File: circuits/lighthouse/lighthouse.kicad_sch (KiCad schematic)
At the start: 45 parts, among them J1 USB_C_Receptacle_USB2.0_14P, J2 Conn_01x03_Socket, Q1 S9013, Q4 SS8050, Q5 SS8050, U10 CP2102-GMR, U2 AMS1117-3.3, U7 ESP32-WROOM-32

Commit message: Ready to go circuit (what a naive thing to say)
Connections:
- net +3.3V: now also R34.2, R8.1
- net +5V: no longer R34.2, R8.1
- net ACTIVE_SCAN: now also U7.34 (RXD0/IO3); no longer U7.30 (IO18)
- net ESP24: now also U7.25 (IO0); no longer U7.24 (IO2)
- net ESP25: now also U7.10 (IO25); no longer U7.25 (IO0)
- net ESP34: now also U7.23 (IO15); no longer U7.34 (RXD0/IO3)
- net ESP35: now also U7.24 (IO2); no longer U7.35 (TXD0/IO1)
- net MQTT_STS: now also U7.26 (IO4); no longer U7.29 (IO5)
- net PIR: now also U7.31 (IO19); no longer U7.8 (IO32)
- net RFID_PW: now also U7.29 (IO5); no longer U7.33 (IO21)
- net RFID_PW_SENSE: now also U7.30 (IO18); no longer U7.36 (IO22)
- net SCAN_DETECTED: now also U7.35 (TXD0/IO1); no longer U7.31 (IO19)
- net WIFI_STS: now also U7.33 (IO21); no longer U7.37 (IO23)
- net at R34.1, SCAN_TGL1.2: now also U7.37 (IO23); no longer U7.6 (IO34)
- net at R8.2, STATUS/SETUP1.2: now also U7.36 (IO22); no longer U7.7 (IO35)
- no-connect marks 25 -> 22
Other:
- moved on the sheet: R21, R34, R8, SCAN_TGL1, STATUS/SETUP1

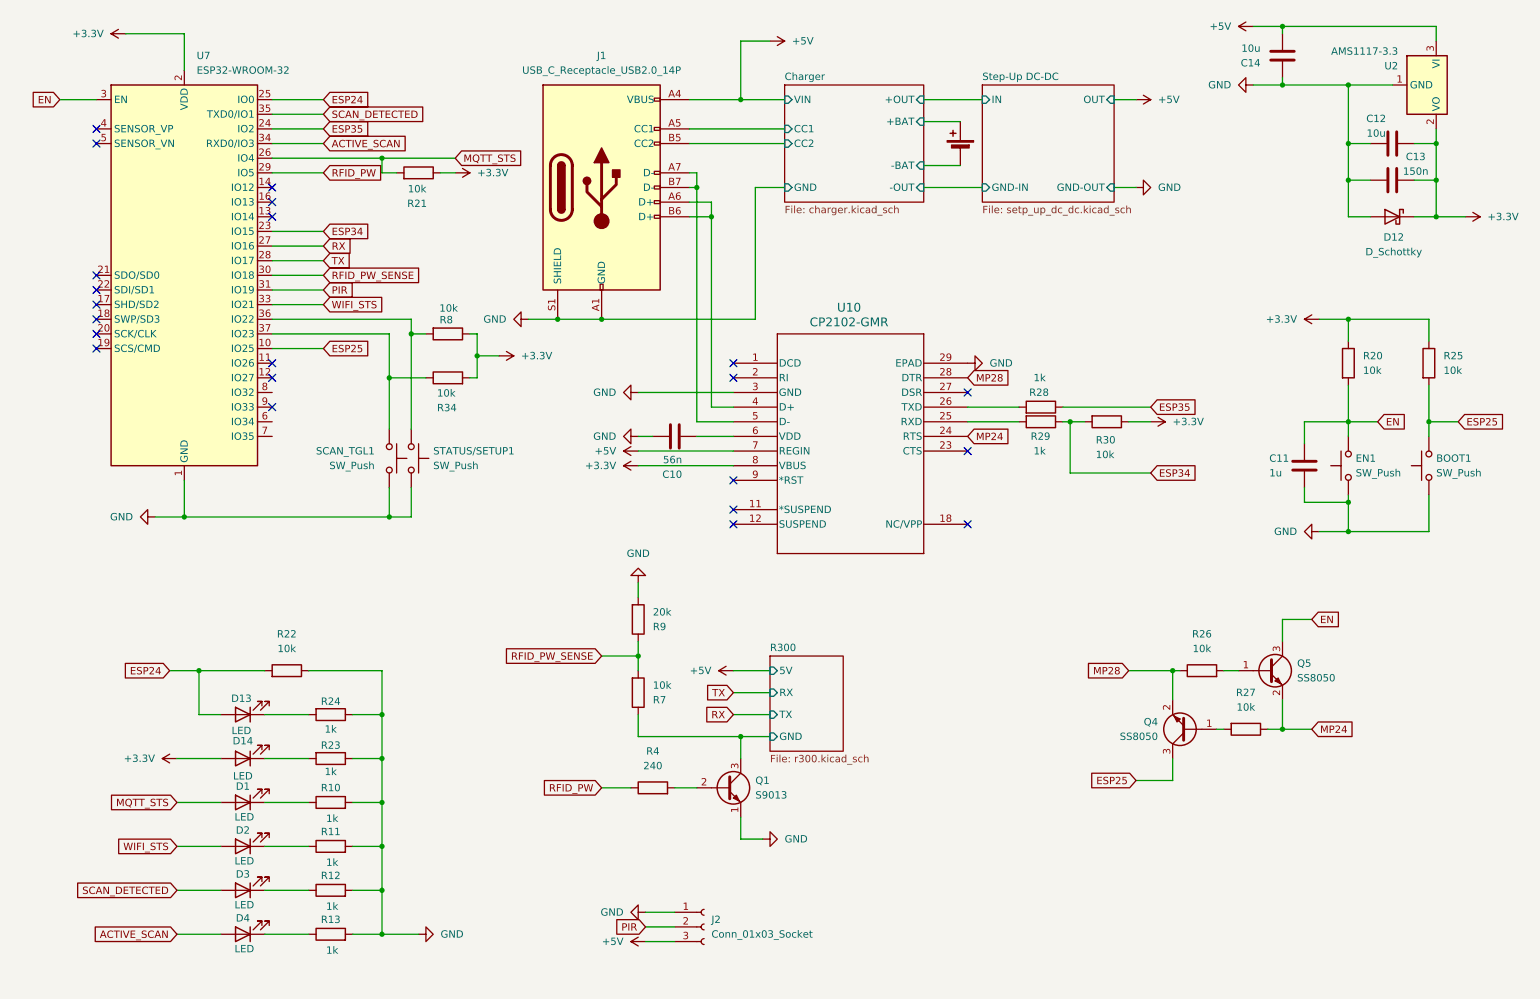
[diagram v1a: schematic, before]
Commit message: Adjusted visa sizes
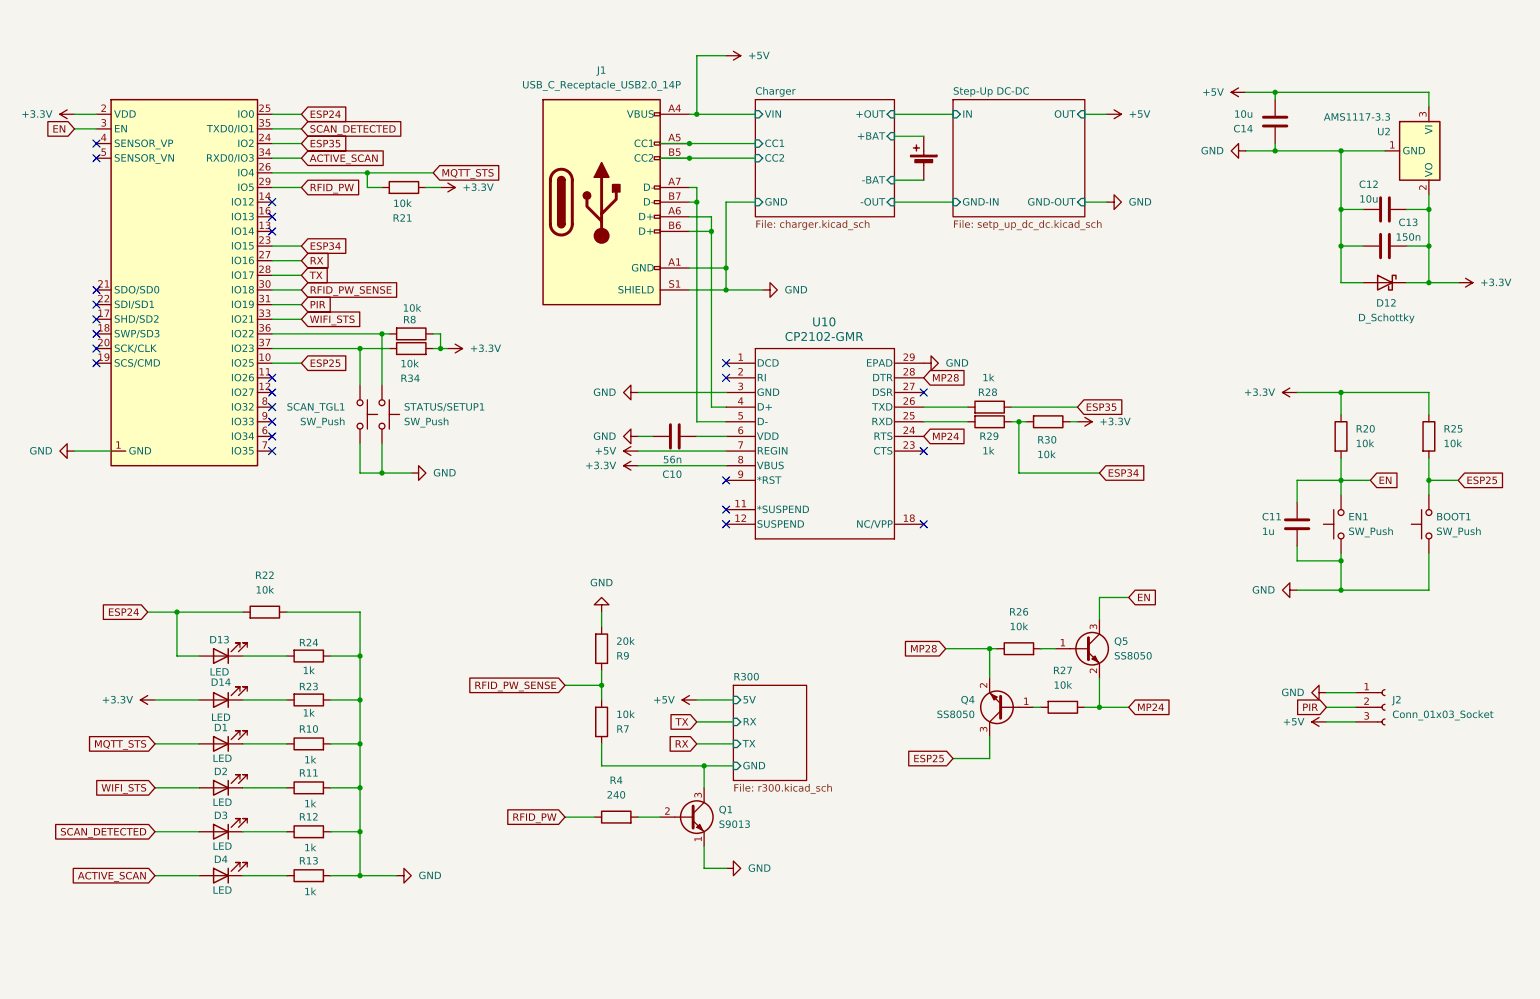
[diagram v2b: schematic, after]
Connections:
- net GND: now also U7.32 (NC)
- no-connect marks 22 -> 25
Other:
- moved on the sheet: BOOT1, C11, C12, C13, C14, D1, D12, D13, D14, D2, D3, D4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

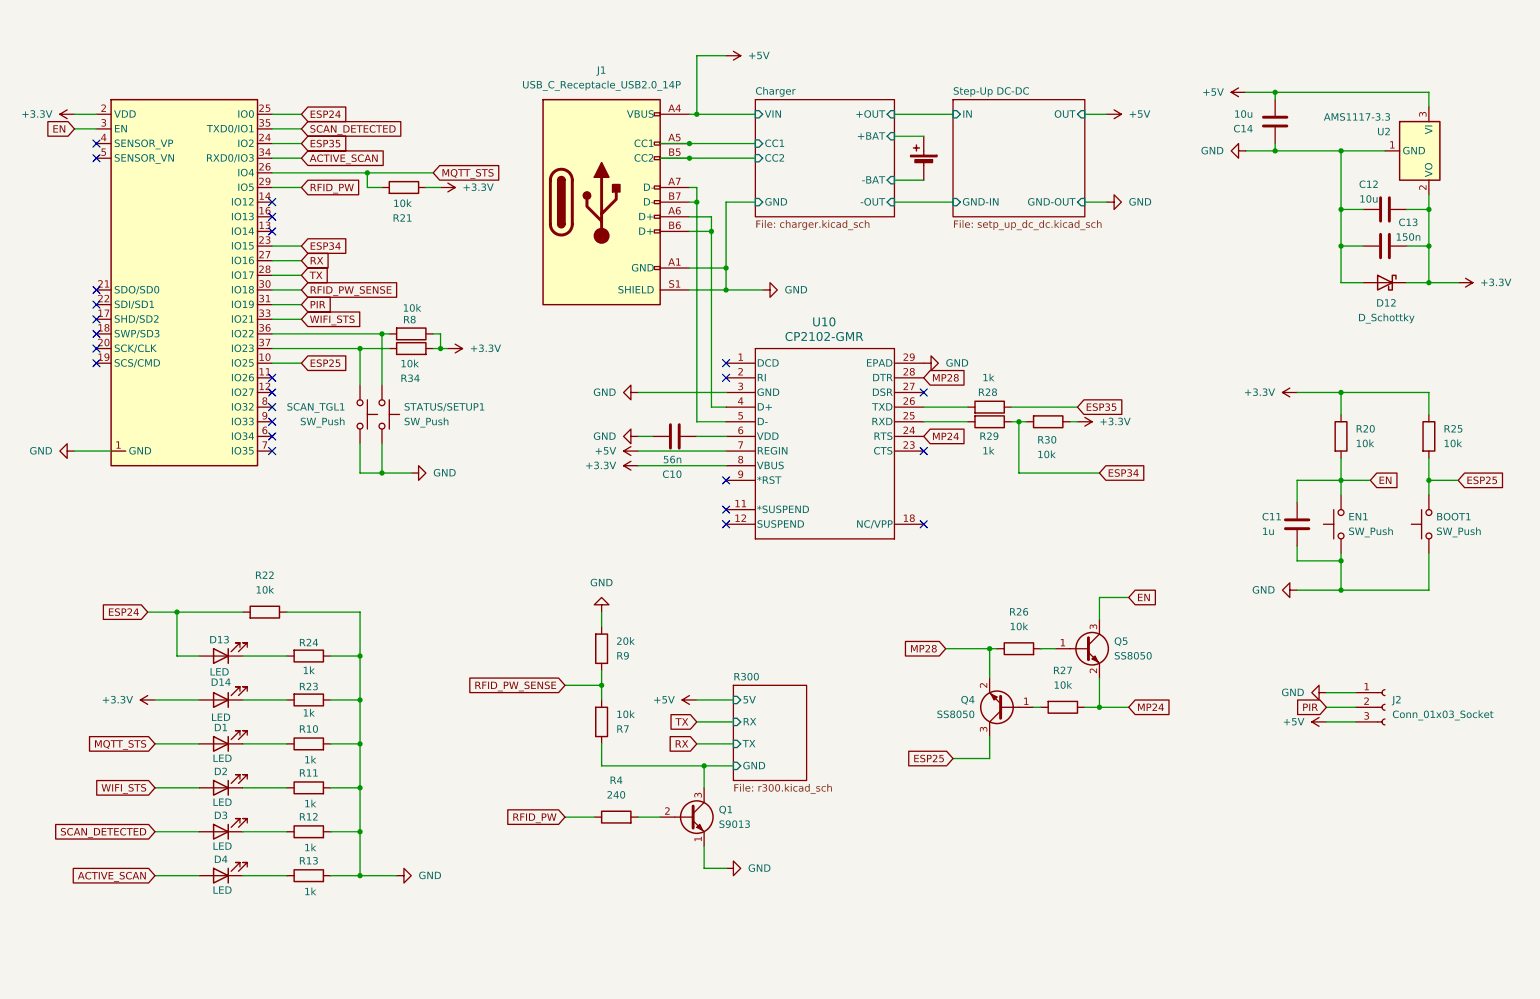
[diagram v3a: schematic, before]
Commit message: Added bulk capacitors, fuses and battery power sense
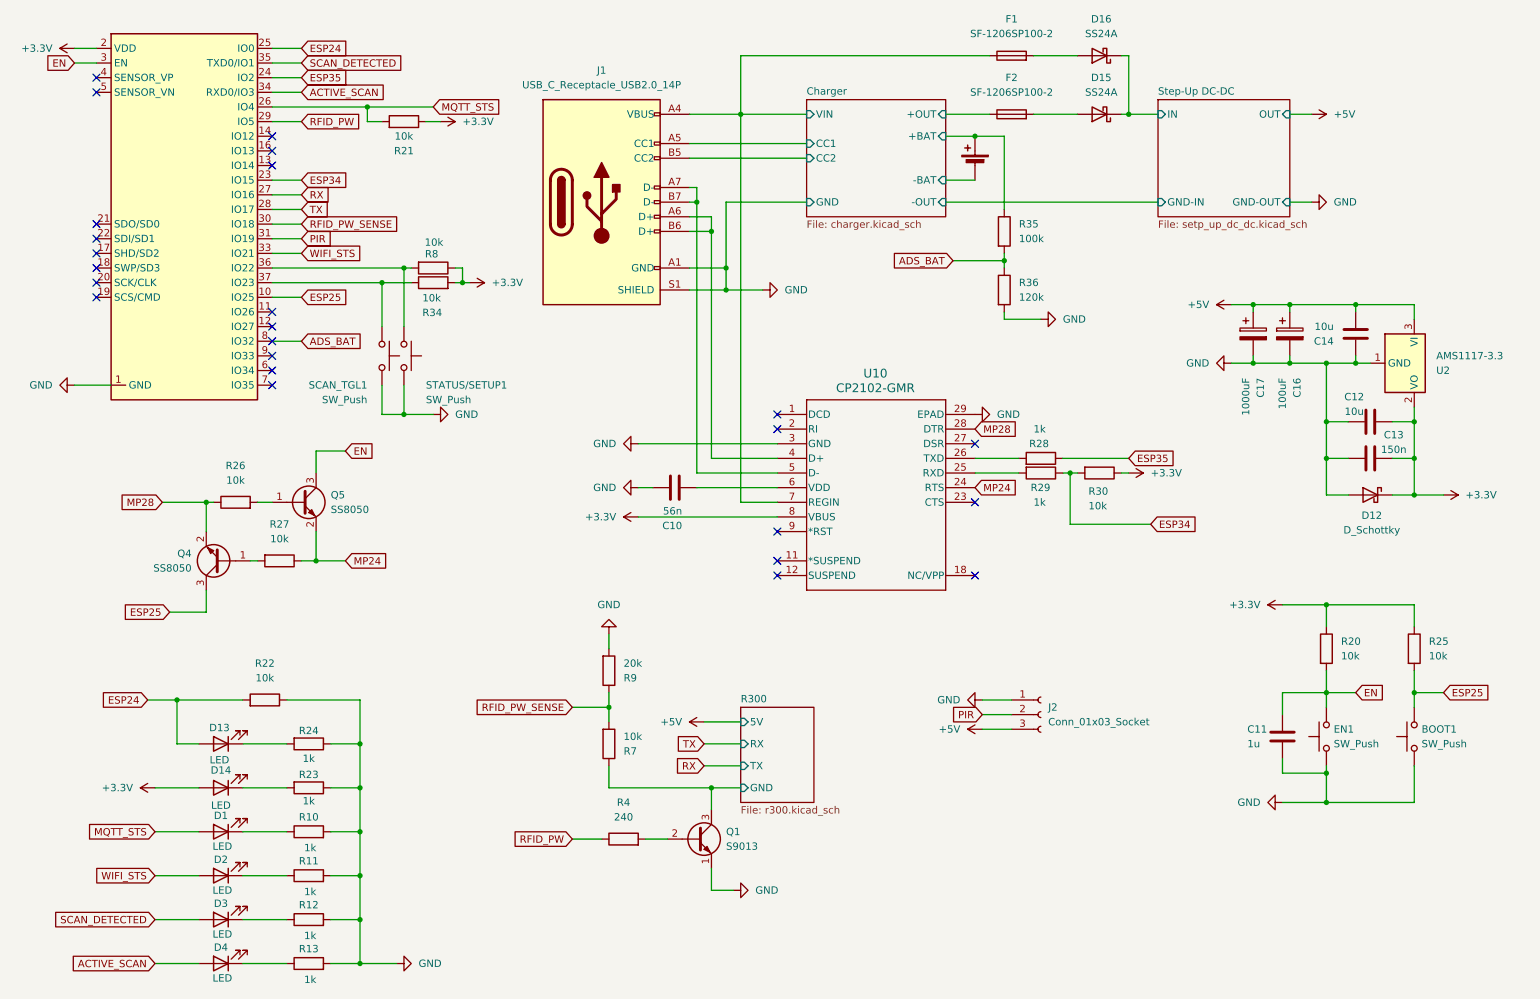
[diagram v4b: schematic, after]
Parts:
- added C16: 100uF, Capacitor_THT:CP_Radial_D6.3mm_P2.50mm, symbol Device:C_Polarized
- added C17: 1000uF, Capacitor_THT:CP_Radial_D10.0mm_P5.00mm, symbol Device:C_Polarized
- added D15, D16: SS24A, Diode_SMD:D_2114_3652Metric_Pad1.85x3.75mm_HandSolder, symbol Device:D_Schottky
- added F1, F2: SF-1206SP100-2, Fuse:Fuse_1206_3216Metric_Pad1.42x1.75mm_HandSolder, symbol Device:Fuse
- added R35: 100k, Resistor_SMD:R_1206_3216Metric_Pad1.30x1.75mm_HandSolder, symbol Device:R
- added R36: 120k, Resistor_SMD:R_1206_3216Metric_Pad1.30x1.75mm_HandSolder, symbol Device:R
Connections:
- net +5V: now also C16.1, C17.1; no longer J1.A4 (VBUS), J1.A9 (VBUS), J1.B4 (VBUS), J1.B9 (VBUS), U10.7 (REGIN)
- net Charger/+BAT: now also R35.1
- net Charger/+OUT: now also F2.1
- net GND: now also C16.2, C17.2, R36.2
- net ADS_BAT: now reaches U7.8 (IO32)
- net ADS_BAT: now also R35.2, R36.1
- new net: D15.2 (A), F2.2
- new net: D16.2 (A), F1.2
- new net Charger/VIN: F1.1, J1.A4 (VBUS), J1.A9 (VBUS), J1.B4 (VBUS), J1.B9 (VBUS), U10.7 (REGIN)
- new net Step-Up DC-DC/IN: D15.1 (K), D16.1 (K)
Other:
- moved on the sheet: BOOT1, C10, C11, C12, C13, C14, D1, D12, D13, D14, D2, D3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

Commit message: Production ready? (most likely not)
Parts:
- D15, D16: footprint Diode_SMD:D_2114_3652Metric_Pad1.85x3.75mm_HandSolder -> Diode_SMD:D_SMA
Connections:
- net +3.3V: now also C16.1
- net +5V: no longer C16.1
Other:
- moved on the sheet: C12, C13, C16, C17, D12
